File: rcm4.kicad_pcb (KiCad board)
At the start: 4 copper layers, 140 x 70 mm, 159 parts, among them Y1 8MHz, Y2 32.768kHz

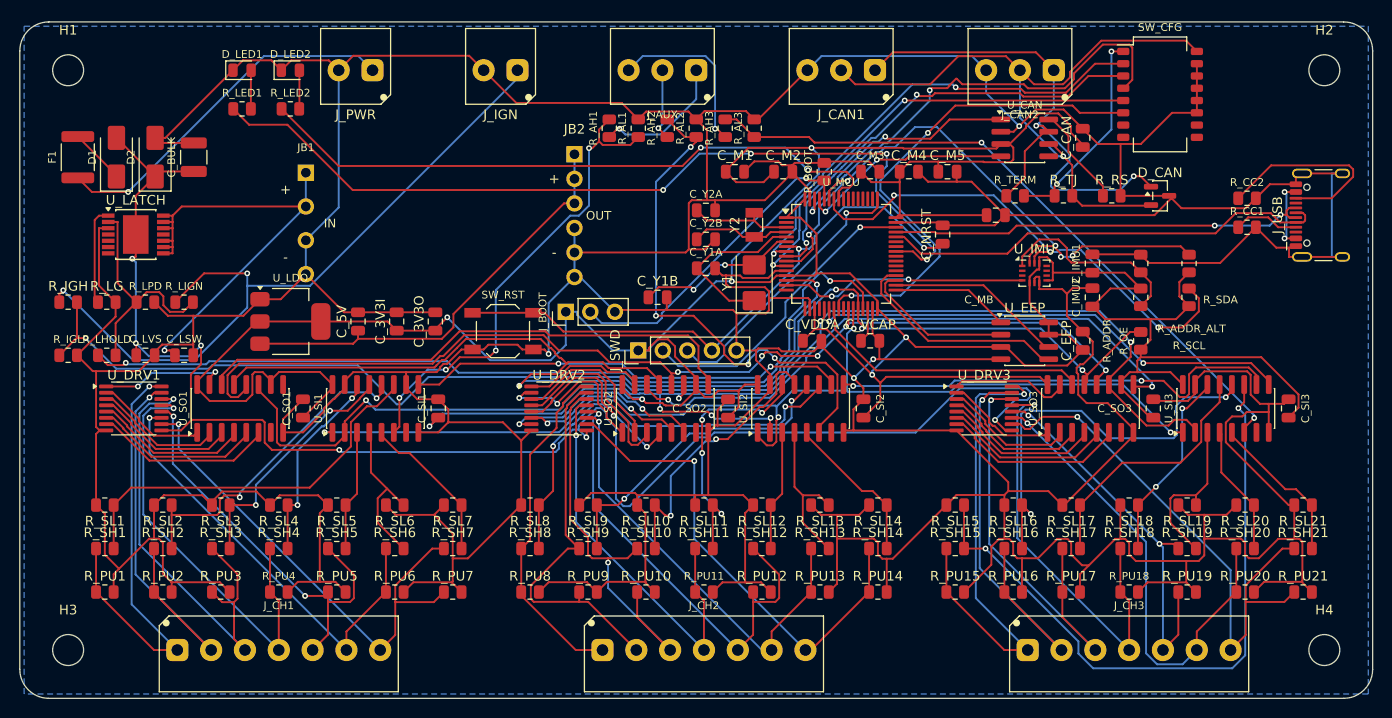
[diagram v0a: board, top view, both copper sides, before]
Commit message: rcm: 4-layer variant with GND left to the pours
Combines both ideas: 4 layers with a solid inner ground plane, AND GND
handed to the copper rather than routed - 117 of its 136 pins never
become traces. IC ground pins stay in the netlist (U_MCU, U_SI, U_IMU,
U_LATCH, U_CAN, U_DRV) because those are boxed in by their own escape
routing and the pour can never reach them. That was the lesson from the
2-layer attempts: leave the easy 90% to copper, route what copper cannot
reach.

  2-layer                  2078 segments, 166 vias, 0 unconnected
  4-layer GND routed       2148 segments, 164 vias, 0 unconnected
  4-layer GND to pours     1766 segments (-15%), 161 vias, 0 ISOLATED PADS

All three are electrically clean with 0 schematic parity errors. This one
has 5 unconnected items but every one is pour-island-to-island, not a
pad - small top-side patches fenced off by traces, with the solid inner
plane carrying current regardless.

Also fixes --no-route-keep prefix matching, which only did exact refs, so
'U_SI' matched nothing.

Needs a stackup, a re-quote and fresh gerbers before it could be ordered.
2-layer board and mfg/ untouched.

Co-Authored-By: Claude Opus 5 <noreply@anthropic.com>
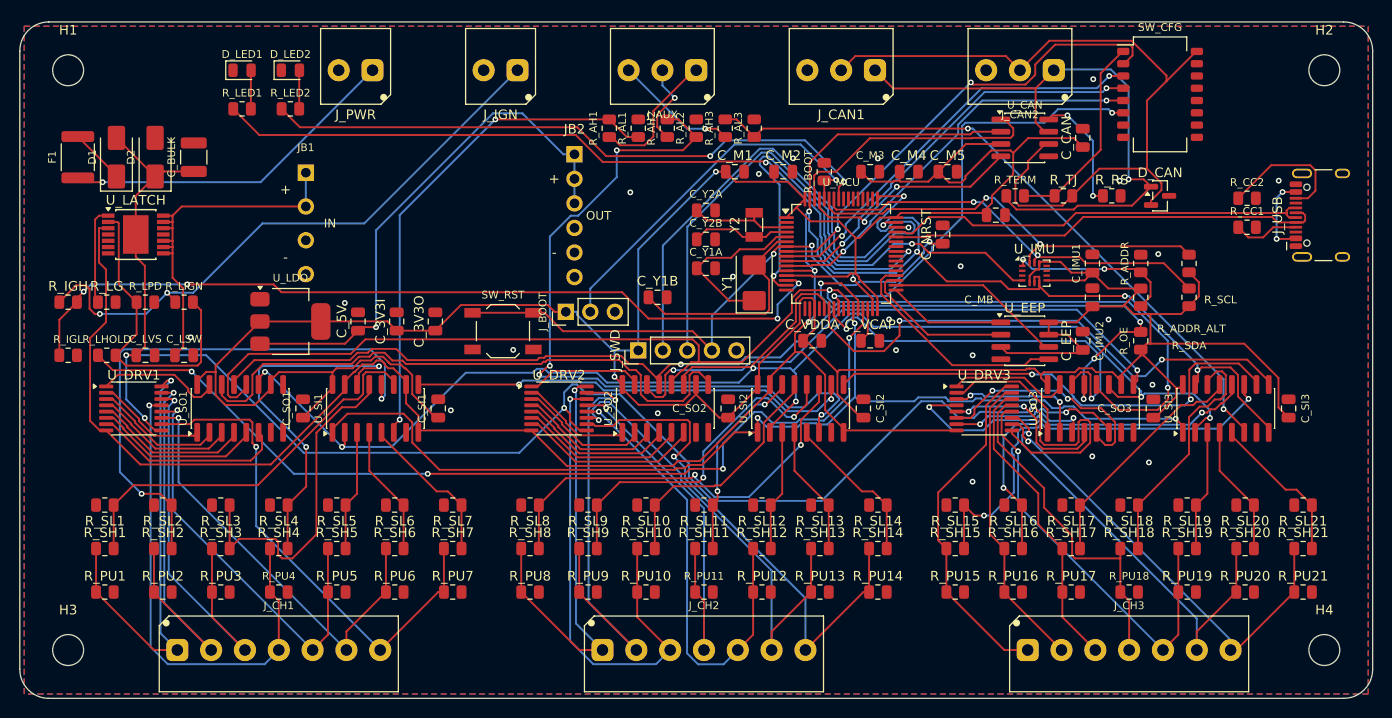
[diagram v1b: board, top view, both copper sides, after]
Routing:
- net GND: track 1010.9 -> 264.1 mm, vias 4 -> 31
- net +3V3: track 429.5 -> 384.7 mm, vias 7 -> 2
- net SWCLK: track 28.8 -> 60.3 mm
- net SR_RCLK: track 108.8 -> 135.3 mm, vias 5 -> 2
- net IMU_INT1: track 25.7 -> 52.0 mm
- net ASNS2: track 54.0 -> 77.5 mm
- net SNS15: track 68.6 -> 45.1 mm
- net SNS2: track 34.1 -> 57.0 mm
- net SWDIO: track 31.7 -> 50.2 mm
- net +12V_P: track 164.2 -> 181.7 mm, vias 6 -> 4
- net SNS4: track 20.7 -> 37.6 mm
- net CH16: track 45.8 -> 31.0 mm, vias 1 -> 0
- net CH15: track 50.6 -> 36.1 mm, vias 1 -> 0
- net LATCH_IGN: track 75.6 -> 62.3 mm
- net CH17: track 44.6 -> 31.5 mm, vias 1 -> 0
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- added copper zone on F.Cu, net GND

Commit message: rcm: examine the 4-layer unconnected items, stitch a floating 43mm2 patch
They are not isolated pads - every pad is connected. They are pour
fragments on the outer layers:

  GND_plane   1 island,  0 orphaned   <- the layer that matters is perfect
  F.Cu       39 islands, 3 orphaned (8.2, 1.25, 0.89 mm2)
  B.Cu       14 islands, 1 orphaned (1.34 mm2)

Found and fixed one real problem: a 43mm2 floating patch on B.Cu, which
was floating because stitch_zone_vias.py only ever examined F.Cu and
never attempted B.Cu islands at all. Now stitched.

Island removal enabled on both outer pours so unconnected copper is
deleted rather than left floating. It did NOT change the DRC count, and I
have not confirmed why - likely KiCad's zone ratsnest wanting same-layer
continuity without crediting the path through the inner plane, but that
is unproven, so the 5 are documented as unexplained-but-benign rather
than declared fine.

Still 0 electrical violations, 0 schematic parity, no unconnected pads.

Co-Authored-By: Claude Opus 5 <noreply@anthropic.com>
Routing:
- net GND: vias 31 -> 32
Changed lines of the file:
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@@
 		(tags "resistor")
 		(property "Reference" "R_SDA"
-			(at -8.500 0.000 0)
+			(at -8.5 0 0)
 			(layer "F.SilkS")
 			(effects
@@
 		(tags "resistor")
 		(property "Reference" "R_SCL"
-			(at -0.250 3.250 0)
+			(at -0.25 3.25 0)
 			(layer "F.SilkS")
 			(effects
@@
 		(tags "capacitor")
 		(property "Reference" "C_IMU2"
-			(at -4.500 0.750 90)
+			(at -4.5 0.75 90)
 			(layer "F.SilkS")
 			(effects
@@
 		(tags "resistor")
 		(property "Reference" "R_ADDR_ALT"
-			(at -3.250 5.250 0)
+			(at -3.25 5.25 0)
 			(layer "F.SilkS")
 			(effects
@@
 		(tags "capacitor")
 		(property "Reference" "C_SO3"
-			(at -0.000 -4.000 0)
+			(at 0 -4 0)
 			(layer "F.SilkS")
 			(effects
@@
 		(tags "capacitor")
 		(property "Reference" "C_MB"
-			(at -1.750 8.750 0)
+			(at -1.75 8.75 0)
 			(layer "F.SilkS")
 			(effects
@@
 		(tags "capacitor")
 		(property "Reference" "C_SI2"
-			(at 0.000 1.750 90)
+			(at 0 1.75 90)
 			(layer "F.SilkS")
 			(effects
@@
 		(tags "capacitor")
 		(property "Reference" "C_SI3"
-			(at 0.000 1.750 90)
+			(at 0 1.75 90)
 			(layer "F.SilkS")
 			(effects
@@
 		(tags "resistor")
 		(property "Reference" "R_OE"
-			(at -0.000 -1.750 90)
+			(at 0 -1.75 90)
 			(layer "F.SilkS")
 			(effects
@@
 		(tags "capacitor")
 		(property "Reference" "C_SO2"
-			(at -0.000 -4.000 0)
+			(at 0 -4 0)
 			(layer "F.SilkS")
 			(effects
@@
 		(size 0.6)
 		(drill 0.3)
+		(layers "F.Cu" "B.Cu")
+		(net "GND")
+	)
+	(via
+		(at 62.418731 26.952514)
+		(size 0.6)
+		(drill 0.3)

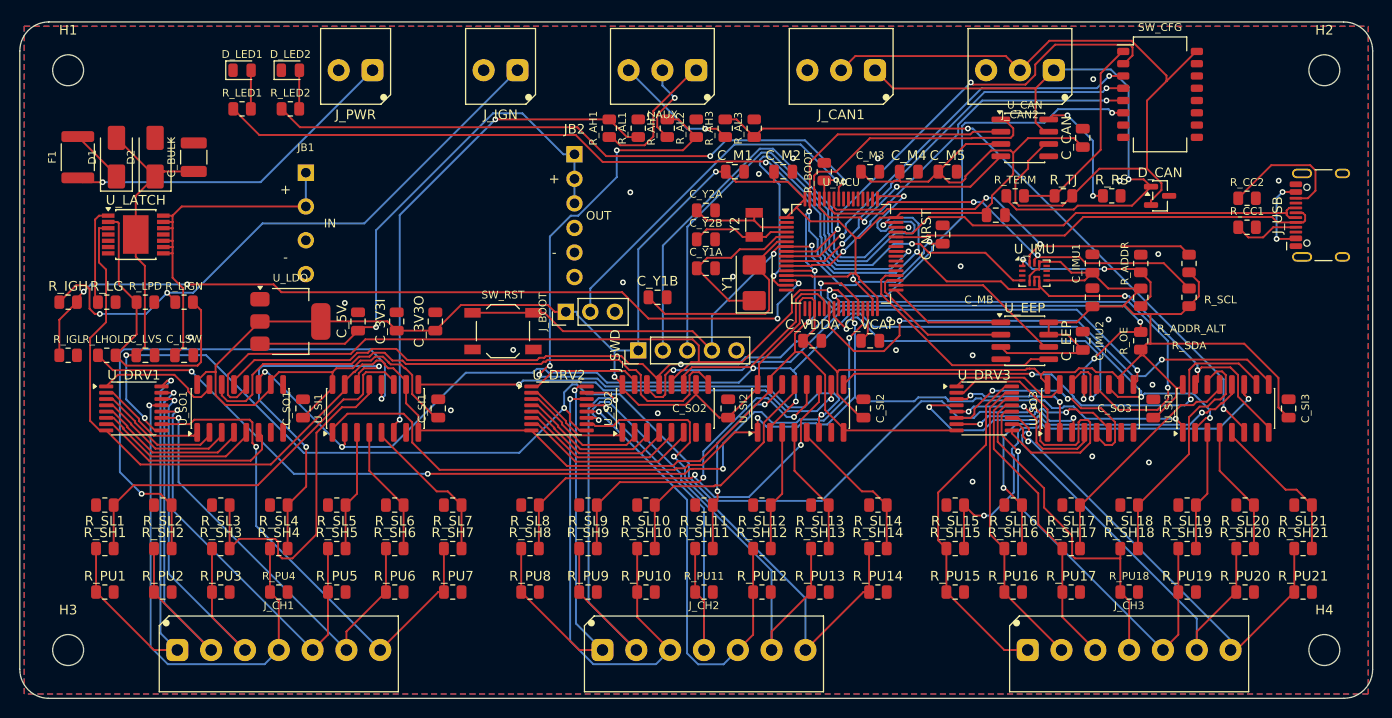
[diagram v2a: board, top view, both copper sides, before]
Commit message: rcm4: silkscreen pass done - converged at 25 cosmetic warnings
13 text-over-text, 12 text-over-pad, across 23 refs, concentrated in the
crowded north-east cluster (U_CAN, J_CAN2, U_MCU) and the tile-1 shift
registers. Same floor the 2-layer board reached.

Both levers are exhausted: ref text is already at 0.8mm, JLC's minimum
height, and relocate_refs reports 0 moves because there is nowhere left
to put anything. The 12 text-over-pad resolve themselves at manufacture
since fabs clip silk off pads; the 13 text-over-text would need a
placement change to clear.

Board is otherwise clean: 0 electrical DRC violations, 0 schematic
parity, no unconnected pads.

Co-Authored-By: Claude Opus 5 <noreply@anthropic.com>
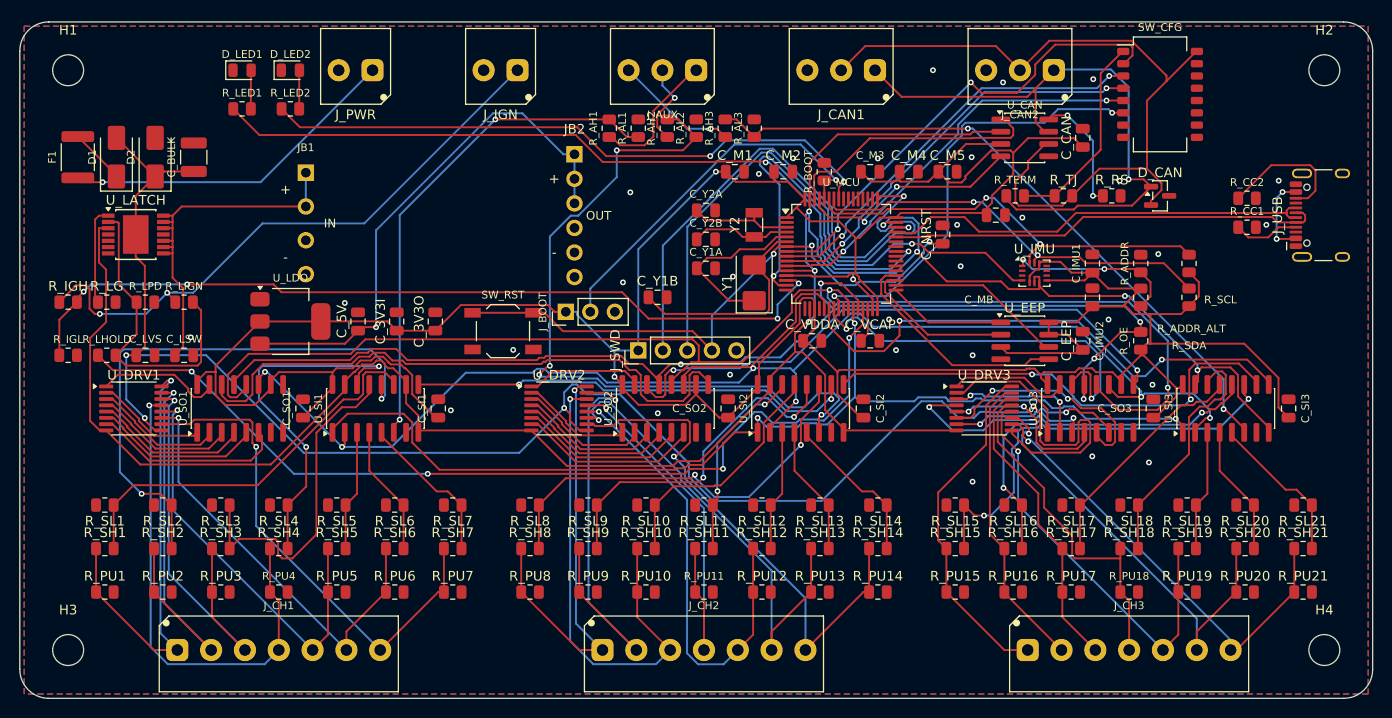
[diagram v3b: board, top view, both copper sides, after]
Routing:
- net CANL: track 80.4 -> 81.2 mm
- net CFG_ROLE: track 48.6 -> 49.3 mm
- net CANH: track 62.8 -> 63.5 mm
- net USB_DP: track 44.7 -> 45.2 mm
- net GND: vias 32 -> 39
